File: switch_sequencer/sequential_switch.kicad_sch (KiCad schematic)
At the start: 2 parts, among them U1 TMUX4051PWR, U2 pico

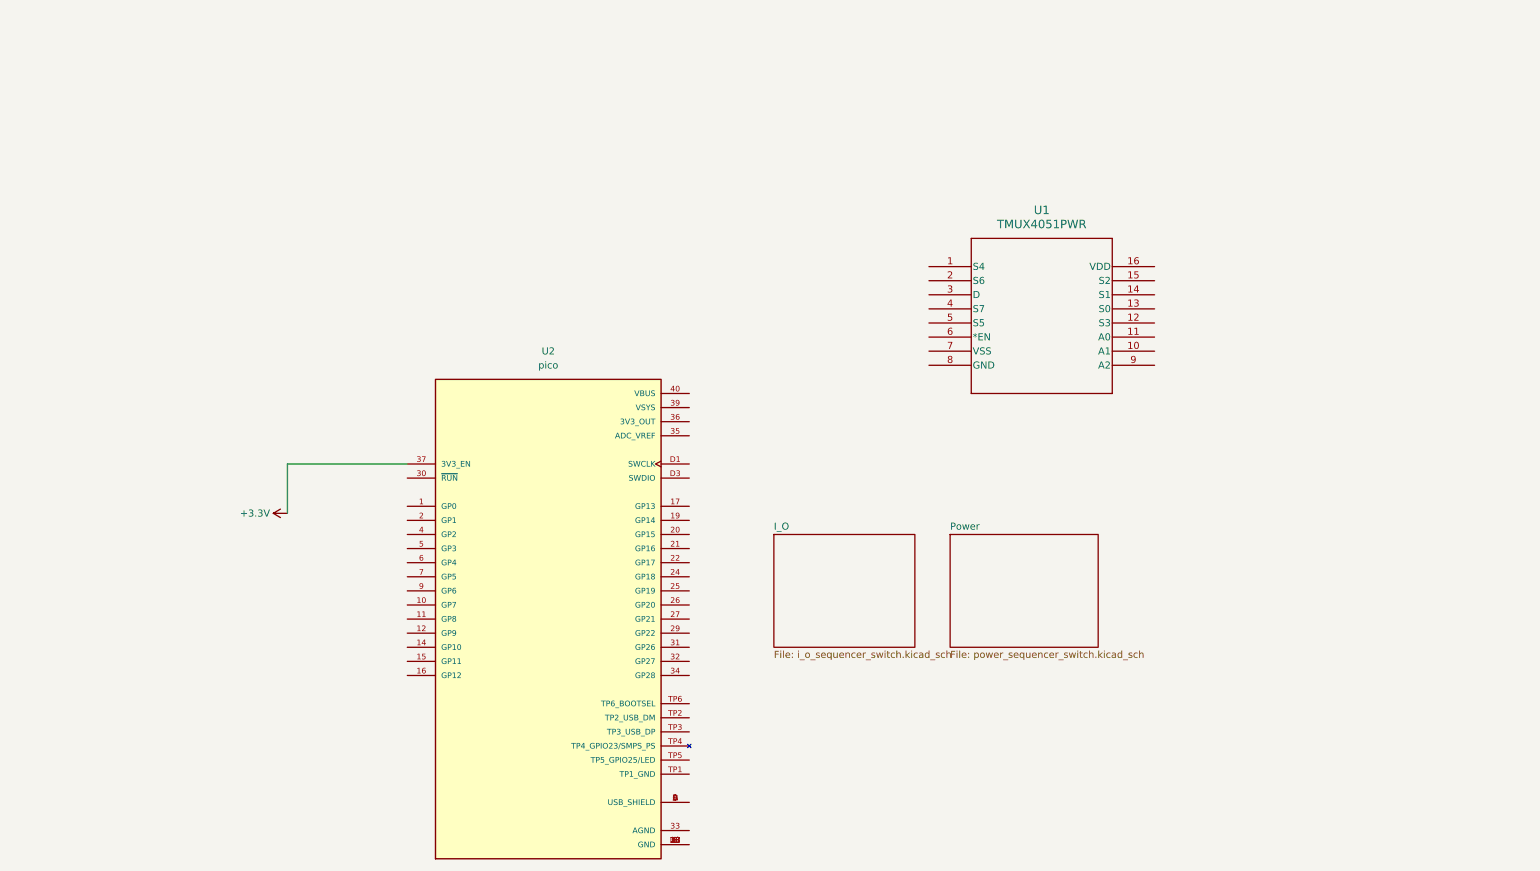
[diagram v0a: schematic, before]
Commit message: Updated schematic of sample and hold, attenuveters, sequential switch
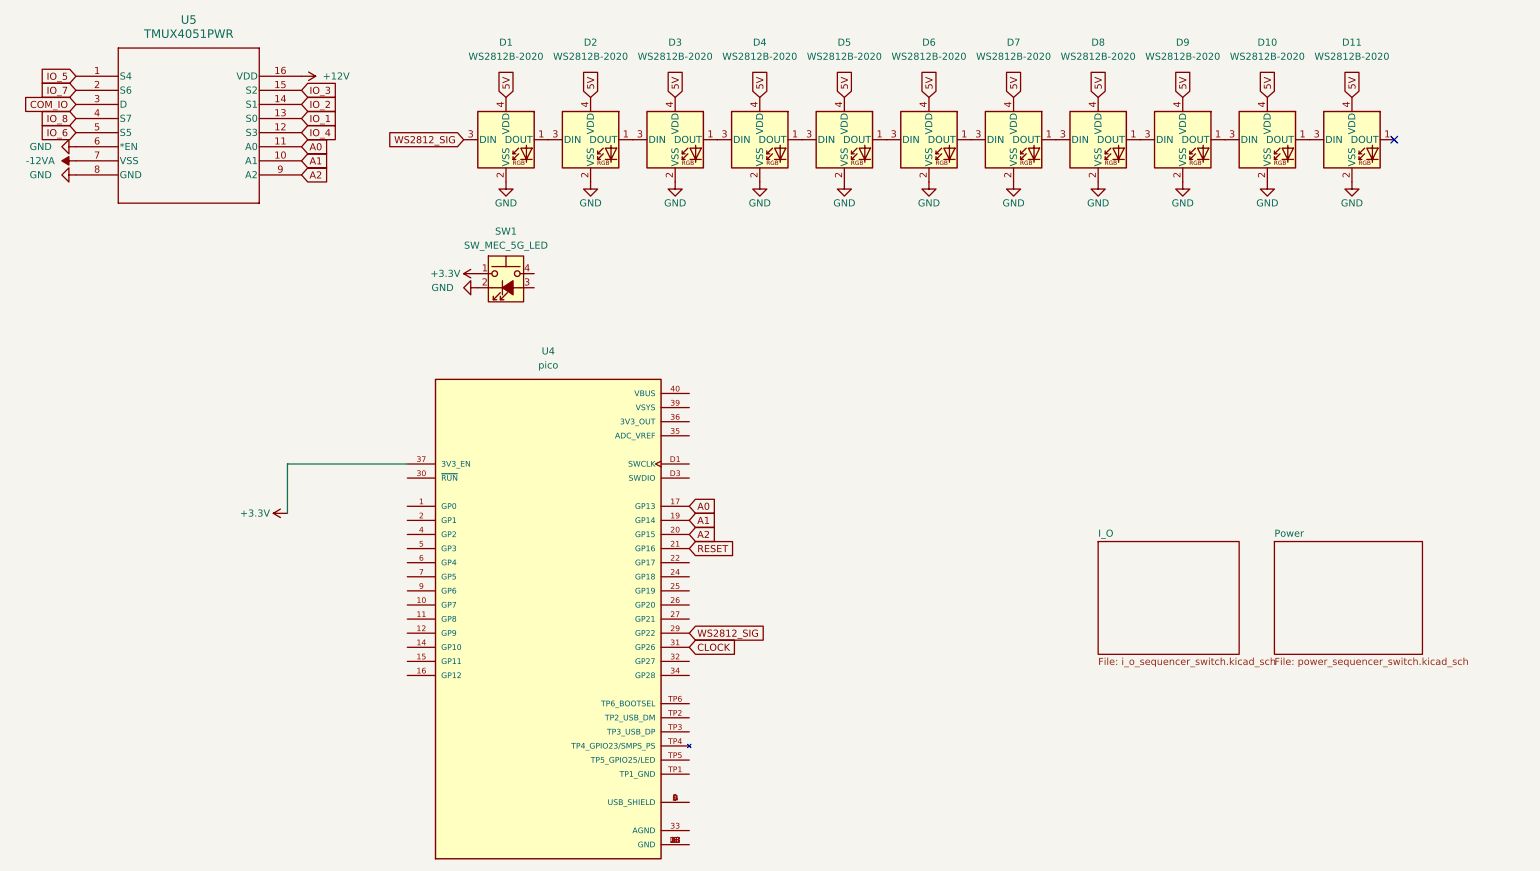
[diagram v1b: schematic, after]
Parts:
- added D1, D10, D11, D2, D3, D4, D5, D6, D7, D8, D9: WS2812B-2020, LED_SMD:LED_WS2812B-2020_PLCC4_2.0x2.0mm, symbol LED:WS2812B-2020
- added SW1: SW_MEC_5G_LED, symbol Switch:SW_MEC_5G_LED
- U5: renamed from U1; footprint TSSOP16_PW_TEX -> TMUX4051:TSSOP16_PW_TEX
- renumbered U2 to U4
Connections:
- net +3.3V: now also SW1.1
- net IO_5: now reaches U5.1 (S4)
- net A1: now reaches U5.10 (A1)
- net A1: now also U4.19 (GP14)
- net A0: now reaches U5.11 (A0)
- net A0: now also U4.17 (GP13)
- net IO_4: now reaches U5.12 (S3)
- net IO_1: now reaches U5.13 (S0)
- net IO_2: now reaches U5.14 (S1)
- net IO_3: now reaches U5.15 (S2)
- net +12V: now reaches U5.16 (VDD)
- net IO_7: now reaches U5.2 (S6)
- net COM_IO: now reaches U5.3 (D)
- net IO_8: now reaches U5.4 (S7)
- net IO_6: now reaches U5.5 (S5)
- net GND: now reaches U5.6 (*EN)
- net GND: now also U5.8 (GND), D1.2 (VSS), D10.2 (VSS), D11.2 (VSS), D2.2 (VSS), D3.2 (VSS), D4.2 (VSS), D5.2 (VSS), D6.2 (VSS), D7.2 (VSS), D8.2 (VSS), D9.2 (VSS), SW1.2
- net -12VA: now reaches U5.7 (VSS)
- net A2: now reaches U5.9 (A2)
- net A2: now also U4.20 (GP15)
- net RESET: now reaches U4.21 (GP16)
- net WS2812_SIG: now reaches U4.29 (GP22)
- net WS2812_SIG: now also D1.3 (DIN)
- net CLOCK: now reaches U4.31 (GP26)
- new net: D2.1 (DOUT), D3.3 (DIN)
- new net: D1.1 (DOUT), D2.3 (DIN)
- new net: D10.3 (DIN), D9.1 (DOUT)
- new net: D8.1 (DOUT), D9.3 (DIN)
- new net: D3.1 (DOUT), D4.3 (DIN)
- new net: D10.1 (DOUT), D11.3 (DIN)
- new net: D5.1 (DOUT), D6.3 (DIN)
- new net: D4.1 (DOUT), D5.3 (DIN)
- new net: D6.1 (DOUT), D7.3 (DIN)
- new net: D7.1 (DOUT), D8.3 (DIN)
- new net 5V: D1.4 (VDD), D10.4 (VDD), D11.4 (VDD), D2.4 (VDD), D3.4 (VDD), D4.4 (VDD), D5.4 (VDD), D6.4 (VDD), D7.4 (VDD), D8.4 (VDD), D9.4 (VDD)
- no-connect marks 0 -> 1
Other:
- moved on the sheet: U5
